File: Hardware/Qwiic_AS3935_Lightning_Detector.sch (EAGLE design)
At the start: 31 parts, among them U1 AS3935

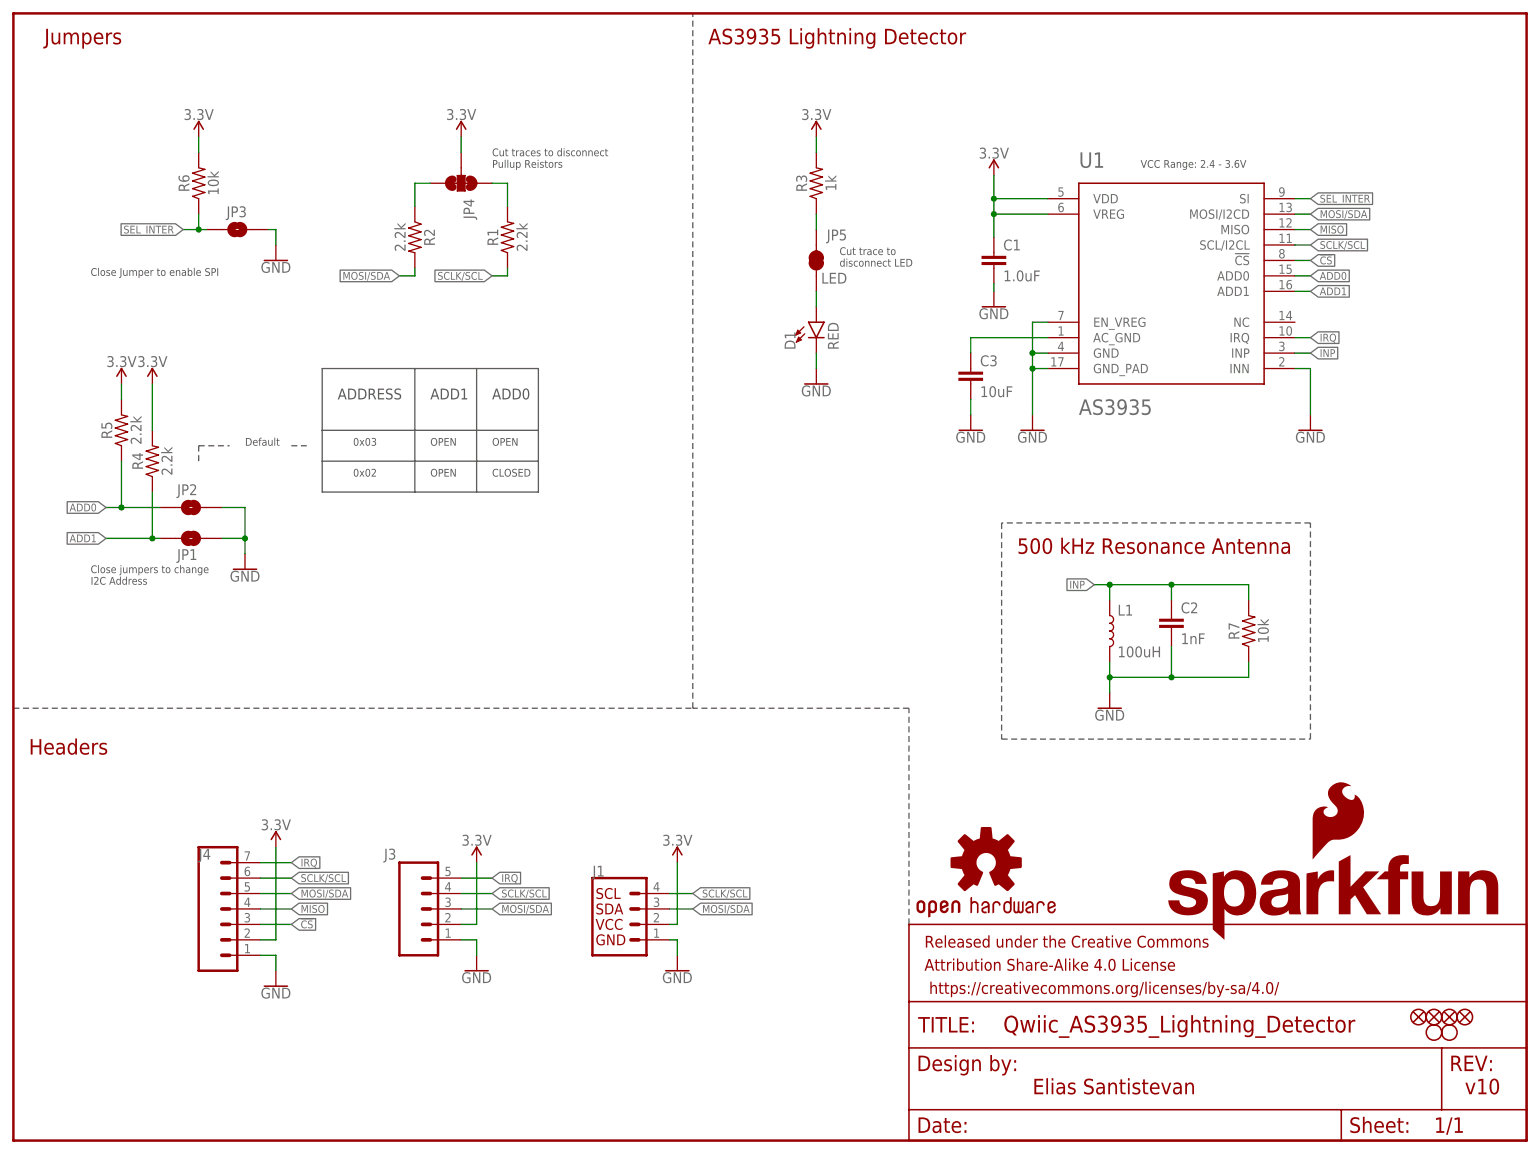
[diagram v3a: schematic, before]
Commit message: Moves drill hits near standoff, moves LED jumper down, renames IRQ net to INT, and adds info on other address options
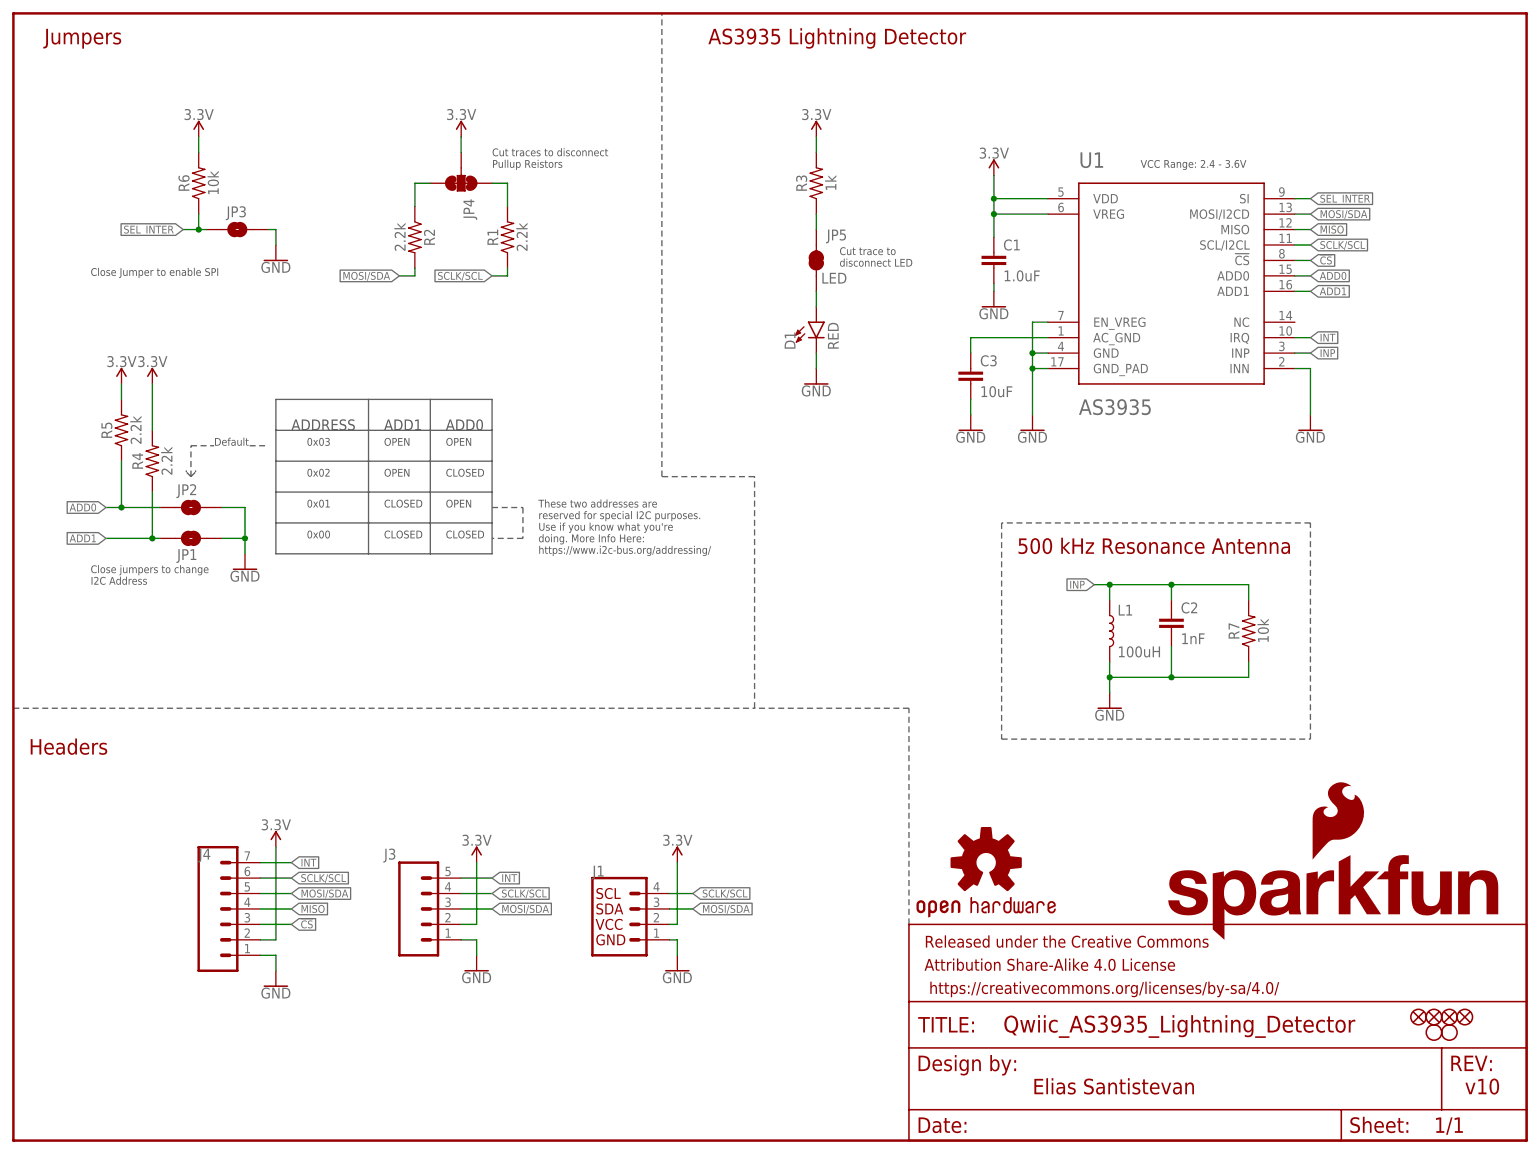
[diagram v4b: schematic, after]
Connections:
- net IRQ renamed INT
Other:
- note added: "0x00"
- note added: "0x01"
- note added: "These two addresses are reserved for special I2C purposes. Use if you know what you're doing. More Info Here: https://www.i2c-bus.org/addressing/"
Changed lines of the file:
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@@
 <text x="167.64" y="7.62" size="2.54" layer="94" font="vector">Elias Santistevan</text>
 <text x="238.76" y="7.62" size="2.54" layer="94" font="vector">v10</text>
-<wire x1="0" y1="71.12" x2="111.76" y2="71.12" width="0.2032" layer="97" style="shortdash"/>
-<wire x1="111.76" y1="71.12" x2="111.76" y2="185.42" width="0.2032" layer="97" style="shortdash"/>
+<wire x1="0" y1="71.12" x2="121.92" y2="71.12" width="0.2032" layer="97" style="shortdash"/>
 <wire x1="147.32" y1="35.56" x2="147.32" y2="71.12" width="0.2032" layer="97" style="shortdash"/>
-<wire x1="147.32" y1="71.12" x2="111.76" y2="71.12" width="0.2032" layer="97" style="shortdash"/>
+<wire x1="147.32" y1="71.12" x2="121.92" y2="71.12" width="0.2032" layer="97" style="shortdash"/>
 <text x="114.3" y="180.34" size="2.54" layer="94" font="vector">AS3935 Lightning Detector</text>
 <text x="5.08" y="180.34" size="2.54" layer="94" font="vector">Jumpers</text>
@@
 <text x="12.7" y="91.44" size="1.27" layer="97" font="vector">Close jumpers to change
 I2C Address</text>
-<wire x1="50.8" y1="127" x2="50.8" y2="116.84" width="0.2032" layer="97"/>
-<wire x1="50.8" y1="116.84" x2="50.8" y2="111.76" width="0.2032" layer="97"/>
-<wire x1="50.8" y1="111.76" x2="50.8" y2="106.68" width="0.2032" layer="97"/>
-<wire x1="86.36" y1="106.68" x2="86.36" y2="111.76" width="0.2032" layer="97"/>
-<wire x1="86.36" y1="111.76" x2="86.36" y2="116.84" width="0.2032" layer="97"/>
-<wire x1="86.36" y1="116.84" x2="86.36" y2="127" width="0.2032" layer="97"/>
-<wire x1="86.36" y1="127" x2="76.2" y2="127" width="0.2032" layer="97"/>
-<wire x1="76.2" y1="127" x2="66.04" y2="127" width="0.2032" layer="97"/>
-<wire x1="66.04" y1="127" x2="50.8" y2="127" width="0.2032" layer="97"/>
-<wire x1="66.04" y1="127" x2="66.04" y2="106.68" width="0.2032" layer="97"/>
-<wire x1="50.8" y1="116.84" x2="86.36" y2="116.84" width="0.2032" layer="97"/>
-<wire x1="50.8" y1="111.76" x2="86.36" y2="111.76" width="0.2032" layer="97"/>
-<wire x1="50.8" y1="106.68" x2="86.36" y2="106.68" width="0.2032" layer="97"/>
-<wire x1="76.2" y1="127" x2="76.2" y2="106.68" width="0.2032" layer="97"/>
-<text x="78.74" y="121.92" size="1.778" layer="97" font="vector" ratio="15">ADD0</text>
-<text x="68.58" y="121.92" size="1.778" layer="97" font="vector" ratio="15">ADD1</text>
-<text x="68.58" y="114.3" size="1.27" layer="97" font="vector">OPEN</text>
-<text x="78.74" y="114.3" size="1.27" layer="97" font="vector">OPEN</text>
-<text x="68.58" y="109.22" size="1.27" layer="97" font="vector">OPEN</text>
-<text x="78.74" y="109.22" size="1.27" layer="97" font="vector">CLOSED</text>
-<text x="53.34" y="121.92" size="1.778" layer="97" font="vector" ratio="15">ADDRESS</text>
-<text x="55.88" y="114.3" size="1.27" layer="97" font="vector">0x03</text>
-<text x="55.88" y="109.22" size="1.27" layer="97" font="vector">0x02</text>
-<text x="38.1" y="114.3" size="1.27" layer="97" font="vector" ratio="15">Default</text>
-<wire x1="30.48" y1="111.76" x2="30.48" y2="114.3" width="0.2032" layer="97" style="shortdash"/>
-<wire x1="30.48" y1="114.3" x2="35.56" y2="114.3" width="0.2032" layer="97" style="shortdash"/>
-<wire x1="45.72" y1="114.3" x2="48.26" y2="114.3" width="0.2032" layer="97" style="shortdash"/>
+<wire x1="43.18" y1="121.92" x2="43.18" y2="116.84" width="0.2032" layer="97"/>
+<wire x1="43.18" y1="116.84" x2="43.18" y2="111.76" width="0.2032" layer="97"/>
+<wire x1="43.18" y1="111.76" x2="43.18" y2="106.68" width="0.2032" layer="97"/>
+<wire x1="43.18" y1="106.68" x2="43.18" y2="101.6" width="0.2032" layer="97"/>
+<wire x1="43.18" y1="101.6" x2="43.18" y2="96.52" width="0.2032" layer="97"/>
+<wire x1="78.74" y1="96.52" x2="78.74" y2="101.6" width="0.2032" layer="97"/>
+<wire x1="78.74" y1="101.6" x2="78.74" y2="106.68" width="0.2032" layer="97"/>
+<wire x1="78.74" y1="106.68" x2="78.74" y2="111.76" width="0.2032" layer="97"/>
+<wire x1="78.74" y1="111.76" x2="78.74" y2="116.84" width="0.2032" layer="97"/>
+<wire x1="78.74" y1="116.84" x2="78.74" y2="121.92" width="0.2032" layer="97"/>
+<wire x1="78.74" y1="121.92" x2="68.58" y2="121.92" width="0.2032" layer="97"/>
+<wire x1="68.58" y1="121.92" x2="58.42" y2="121.92" width="0.2032" layer="97"/>
+<wire x1="58.42" y1="121.92" x2="43.18" y2="121.92" width="0.2032" layer="97"/>
+<wire x1="58.42" y1="121.92" x2="58.42" y2="106.68" width="0.2032" layer="97"/>
+<wire x1="43.18" y1="116.84" x2="78.74" y2="116.84" width="0.2032" layer="97"/>
+<wire x1="43.18" y1="111.76" x2="78.74" y2="111.76" width="0.2032" layer="97"/>
+<wire x1="68.58" y1="121.92" x2="68.58" y2="106.68" width="0.2032" layer="97"/>
+<text x="71.12" y="116.84" size="1.778" layer="97" font="vector" ratio="15">ADD0</text>
+<text x="60.96" y="116.84" size="1.778" layer="97" font="vector" ratio="15">ADD1</text>
+<text x="60.96" y="114.3" size="1.27" layer="97" font="vector">OPEN</text>
+<text x="71.12" y="114.3" size="1.27" layer="97" font="vector">OPEN</text>
+<text x="60.96" y="109.22" size="1.27" layer="97" font="vector">OPEN</text>
+<text x="71.12" y="109.22" size="1.27" layer="97" font="vector">CLOSED</text>
+<text x="45.72" y="116.84" size="1.778" layer="97" font="vector" ratio="15">ADDRESS</text>
+<text x="48.26" y="114.3" size="1.27" layer="97" font="vector">0x03</text>
+<text x="48.26" y="109.22" size="1.27" layer="97" font="vector">0x02</text>
+<text x="33.02" y="114.3" size="1.27" layer="97" font="vector" ratio="15">Default</text>
+<wire x1="29.21" y1="109.22" x2="29.21" y2="114.3" width="0.2032" layer="97" style="shortdash"/>
+<wire x1="29.21" y1="114.3" x2="33.02" y2="114.3" width="0.2032" layer="97" style="shortdash"/>
+<wire x1="38.862" y1="114.3" x2="41.402" y2="114.3" width="0.2032" layer="97" style="shortdash"/>
 <text x="185.42" y="160.02" size="1.27" layer="97">VCC Range: 2.4 - 3.6V</text>
 <text x="135.89" y="143.764" size="1.27" layer="97" font="vector">Cut trace to
 disconnect LED</text>
+<wire x1="43.18" y1="106.68" x2="58.42" y2="106.68" width="0.2032" layer="97"/>
+<wire x1="58.42" y1="106.68" x2="68.58" y2="106.68" width="0.2032" layer="97"/>
+<wire x1="68.58" y1="106.68" x2="78.74" y2="106.68" width="0.2032" layer="97"/>
+<wire x1="43.18" y1="101.6" x2="58.42" y2="101.6" width="0.2032" layer="97"/>
+<wire x1="58.42" y1="101.6" x2="68.58" y2="101.6" width="0.2032" layer="97"/>
+<wire x1="68.58" y1="101.6" x2="78.74" y2="101.6" width="0.2032" layer="97"/>
+<wire x1="58.42" y1="106.68" x2="58.42" y2="101.6" width="0.2032" layer="97"/>
+<wire x1="43.18" y1="96.52" x2="58.42" y2="96.52" width="0.2032" layer="97"/>
+<wire x1="58.42" y1="101.6" x2="58.42" y2="96.52" width="0.2032" layer="97"/>
+<wire x1="58.42" y1="96.52" x2="68.58" y2="96.52" width="0.2032" layer="97"/>
+<text x="48.26" y="104.14" size="1.27" layer="97" font="vector">0x01</text>
+<text x="48.26" y="99.06" size="1.27" layer="97" font="vector">0x00</text>
+<wire x1="68.58" y1="96.52" x2="78.74" y2="96.52" width="0.2032" layer="97"/>
+<wire x1="68.58" y1="106.68" x2="68.58" y2="101.6" width="0.2032" layer="97"/>
+<wire x1="68.58" y1="101.6" x2="68.58" y2="96.52" width="0.2032" layer="97"/>
+<text x="71.12" y="104.14" size="1.27" layer="97" font="vector">OPEN</text>
+<text x="60.96" y="104.14" size="1.27" layer="97" font="vector">CLOSED</text>
+<text x="60.96" y="99.06" size="1.27" layer="97" font="vector">CLOSED</text>
+<text x="71.12" y="99.06" size="1.27" layer="97" font="vector">CLOSED</text>
+<wire x1="78.74" y1="104.14" x2="83.82" y2="104.14" width="0.2032" layer="97" style="shortdash"/>
+<wire x1="83.82" y1="104.14" x2="83.82" y2="99.06" width="0.2032" layer="97" style="shortdash"/>
+<wire x1="83.82" y1="99.06" x2="78.74" y2="99.06" width="0.2032" layer="97" style="shortdash"/>
+<text x="86.36" y="96.52" size="1.27" layer="97" font="vector">These two addresses are
+reserved for special I2C purposes.
+Use if you know what you're
+doing. More Info Here:
+https://www.i2c-bus.org/addressing/</text>
+<wire x1="121.92" y1="71.12" x2="121.92" y2="109.22" width="0.2032" layer="97" style="shortdash"/>
+<wire x1="121.92" y1="109.22" x2="106.68" y2="109.22" width="0.2032" layer="97" style="shortdash"/>
+<wire x1="106.68" y1="109.22" x2="106.68" y2="185.42" width="0.2032" layer="97" style="shortdash"/>
+<wire x1="29.21" y1="109.22" x2="29.972" y2="109.982" width="0.2032" layer="97" style="shortdash"/>
+<wire x1="29.972" y1="109.982" x2="29.972" y2="110.236" width="0.2032" layer="97" style="shortdash"/>
+<wire x1="29.21" y1="109.22" x2="28.448" y2="109.982" width="0.2032" layer="97" style="shortdash"/>
+<wire x1="28.448" y1="109.982" x2="28.448" y2="110.236" width="0.2032" layer="97" style="shortdash"/>
 </plain>
 <instances>
@@
 </segment>
 </net>
-<net name="IRQ" class="0">
+<net name="INT" class="0">
 <segment>
 <pinref part="J4" gate="J1" pin="7"/>
